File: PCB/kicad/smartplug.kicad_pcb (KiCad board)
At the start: 2 copper layers, 97.5 x 99 mm, 108 parts, among them IC9 534998-4, J1 1935174, J12 M50-3530242, J2 1935174, J3 826629-4, J7 Conn_01x01, J8 Conn_01x01, J9 USB_C_Receptacle_USB2.0, Y1 32MHZ

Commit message: PCB 1.0: - Corrected 5V generation - Corrected USB ESD protection - Replaced USB type-C with micro type-B
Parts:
- removed IC1: ~, alecot:SOT95P280X145-6N
- removed J9: USB_C_Receptacle_USB2.0, Connector_USB:USB_C_Receptacle_JAE_DX07S016JA1R1500
- removed R13: 0R, alecot:ERJ3EKF1000V
- removed R17: 10K, alecot:RESC1608X55N
- removed R19: 1M, alecot:RESC1608X55N
- removed R2: 22.1K, alecot:RESC1608X55N
- removed R20, R21: 5.1K, alecot:RESC1608X55N
- removed R3: 88.7K, alecot:RESC1608X55N
- added J4: 10118192-0002LF, alecot:101181920002LF, F.Cu at (175.4, 116.9)
- added PS2: VXO7805-1000, alecot:VXO780121000, F.Cu at (168.3, 71.9)
- C2: value 2.2u -> 10u; footprint alecot:CAPC3116X180N -> alecot:CAPC3225X270N
- C3: value 0.1u -> 22u; footprint alecot:CAPC1005X55N -> alecot:CAPC1608X90N
- C4: value 10u -> 4.7u; footprint alecot:CAPC3225X270N -> alecot:CAPC2012X135N
- L1: value 4.7u -> 12u; footprint alecot:LQM21PHR47NG0D -> alecot:1227ASH100MP2
- moved C4 14.2 mm to (173.6, 63.8), turned to 0 degrees
- moved L1 12.0 mm to (175.8, 67.5)
- moved C3 9.81 mm to (175.5, 77.6), turned to 180 degrees
- moved C2 8.33 mm to (175.8, 72.5), turned to 90 degrees
- moved C1 2.20 mm to (155.7, 76.1)
- moved G*** 1.43 mm to (169.4, 111.8)
- moved IC7 0.80 mm to (164.3, 117.2), turned to 0 degrees
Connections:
- C2 pad 2: VBUS -> Net-(PS2-+VIN)
- C3 pad 1: Net-(IC1-CB) -> GND
- C3 pad 2: Net-(IC1-SW) -> +5V
- C4 pad 2: +5V -> VBUS
- IC7 pad 1: USB_CONN_D- -> USB_D+
- IC7 pad 4: USB_D+ -> USB_CONN_D-
- L1 pad 1: Net-(IC1-SW) -> VBUS
- L1 pad 2: +5V -> Net-(PS2-+VIN)
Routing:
- net Net-(J9-SHIELD): track 24.8 -> 0.00 mm
- net +5V: track 136.6 -> 122.8 mm, vias 4 -> 3
- net GND: track 75.5 -> 67.4 mm, vias 58 -> 52
- net Net-(PS2-+VIN): track 0.00 -> 6.98 mm
- net Net-(IC1-EN): track 5.22 -> 0.00 mm
- net VBUS: track 45.9 -> 40.9 mm
- net Net-(IC1-SW): track 4.60 -> 0.00 mm
- net USB_D+: track 14.1 -> 10.1 mm
- net Net-(IC1-FB): track 3.59 -> 0.00 mm
- net Net-(J9-CC2): track 3.02 -> 0.00 mm
- net Net-(J9-CC1): track 3.02 -> 0.00 mm
- net USB_D-: track 11.0 -> 8.82 mm, vias 2 -> 0
- net USB_CONN_D+: track 6.24 -> 8.24 mm
- net Net-(IC1-CB): track 1.96 -> 0.00 mm
- net USB_CONN_D-: track 9.00 -> 8.22 mm
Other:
- board text added: "Smartplug V1.0 03/23 cotaa"
- board text removed: "Smartplug V0.0 08/23 cotaa"

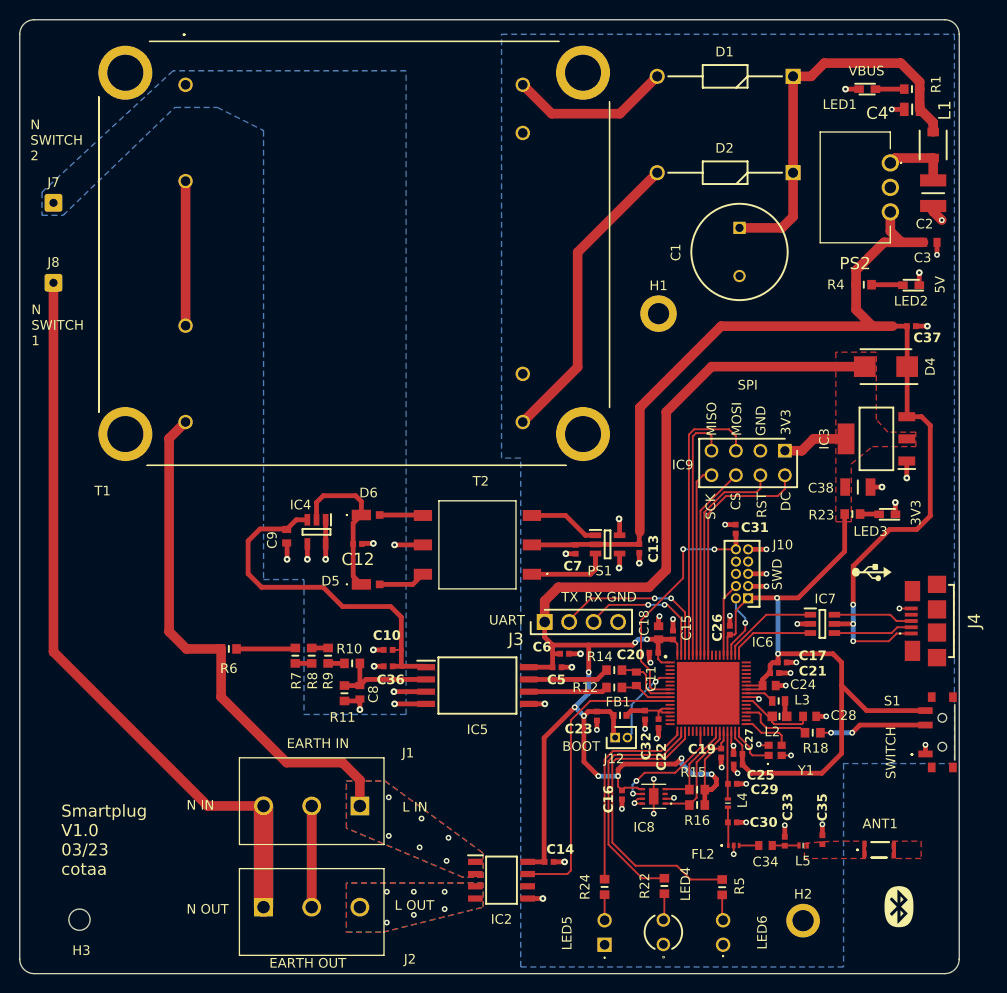
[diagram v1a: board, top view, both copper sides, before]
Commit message: Antenna chip replaced with antenna trace on PCB Switch replaced with button Added GND test point Added PD res on Boot pin Added NRST capacitor
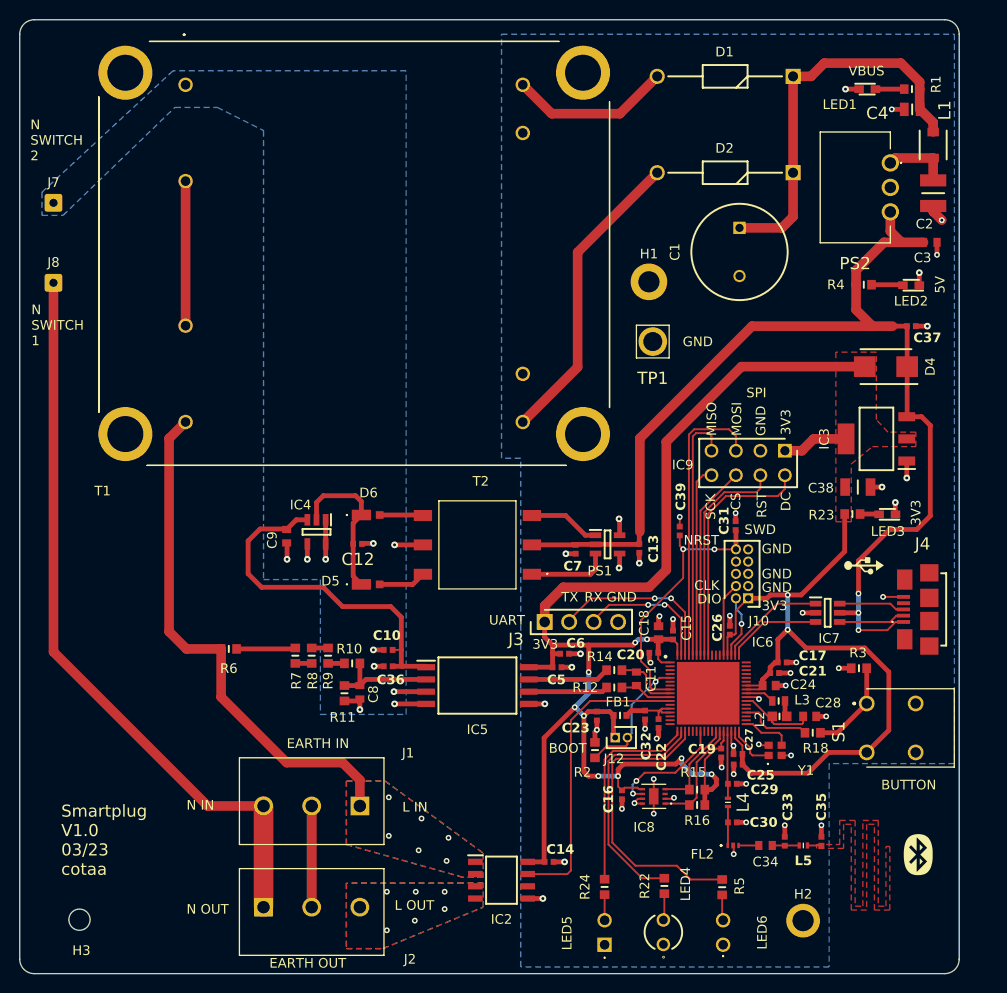
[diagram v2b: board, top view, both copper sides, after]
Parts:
- removed ANT1: ANT3216LL00R2400A, alecot:ANT3216LL00R2400A
- added C39: 0.1u, alecot:CAPC1005X55N, F.Cu at (149.5, 107.6)
- added R2: 10K, alecot:RESC1608X55N, F.Cu at (140.7, 130.3)
- added R3: 10K, alecot:RESC1608X55N, F.Cu at (168.1, 121.8)
- added TP1: 5023, alecot:5023, F.Cu at (146.7, 87.9)
- C35: value n.f. -> 1.2p
- L5: value 0L -> 3.6n
- S1: value PCM12SMTR -> 800SP9B5M6RE; footprint alecot:PCM12SMTR -> alecot:800SP9B5M6RE
- moved S1 8.40 mm to (168.9, 125.5), turned to -90 degrees
- moved G*** 5.76 mm to (174.2, 141.1)
- moved H1 3.45 mm to (146.3, 81.7)
- moved J4 1.44 mm to (174.6, 115.7)
- moved IC7 1.27 mm to (164.8, 116.0)
- moved G*** 1.06 mm to (168.6, 111.1)
- moved C31 0.36 mm to (155.3, 107.0)
- moved C35 0.19 mm to (164.2, 139.8), turned to -90 degrees
- moved L4 0.08 mm to (154.5, 135.7)
- moved FL2 0.06 mm to (155.0, 140.2)
- turned L5 to 0 degrees
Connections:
- C35 pad 1: /interfaces/FEED -> GND
- C35 pad 2: GND -> /interfaces/FEED
- L5 pad 1: /interfaces/FEED -> /interfaces/MATCH_IMP
- L5 pad 2: /interfaces/MATCH_IMP -> /interfaces/FEED
- S1 pad 1: GND -> SW_SWITCH
- S1 pad 2: SW_SWITCH -> GND
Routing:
- net BOOT: track 8.74 -> 13.4 mm
- net +5V: track 122.8 -> 118.2 mm
- net +3.3V: track 235.8 -> 233.0 mm
- net GND: track 67.4 -> 65.1 mm, vias 52 -> 50
- net NRST: track 25.8 -> 27.4 mm
- net SW_SWITCH: track 11.2 -> 9.72 mm, vias 2 -> 0
- net /interfaces/FEED: track 0.00 -> 1.46 mm
- net USB_CONN_D+: track 8.24 -> 6.87 mm
- net USB_CONN_D-: track 8.22 -> 6.89 mm
- net USB_D+: track 10.1 -> 11.1 mm
- net USB_D-: track 8.82 -> 9.85 mm
- removed copper zone on F.Cu, net /interfaces/SOLD
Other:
- board text added: "BUTTON"
- board text added: "CLK"
- board text added: "DIO"
- board text added: "NRST"
- board text removed: "SWITCH"

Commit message: Modified year silk
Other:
- board text added: "Smartplug V1.0 03/24 cotaa"
- board text removed: "Smartplug V1.0 03/23 cotaa"
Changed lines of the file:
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@@
     (effects (font (size 1 1) (thickness 0.15)) (justify left bottom))
   )
-  (gr_text "Smartplug\nV1.0\n03/23\ncotaa" (at 85.3 143.4) (layer "F.SilkS")
+  (gr_text "Smartplug\nV1.0\n03/24\ncotaa" (at 85.3 143.4) (layer "F.SilkS")
     (effects (font (size 1.25 1.25) (thickness 0.2)) (justify left bottom))
   )

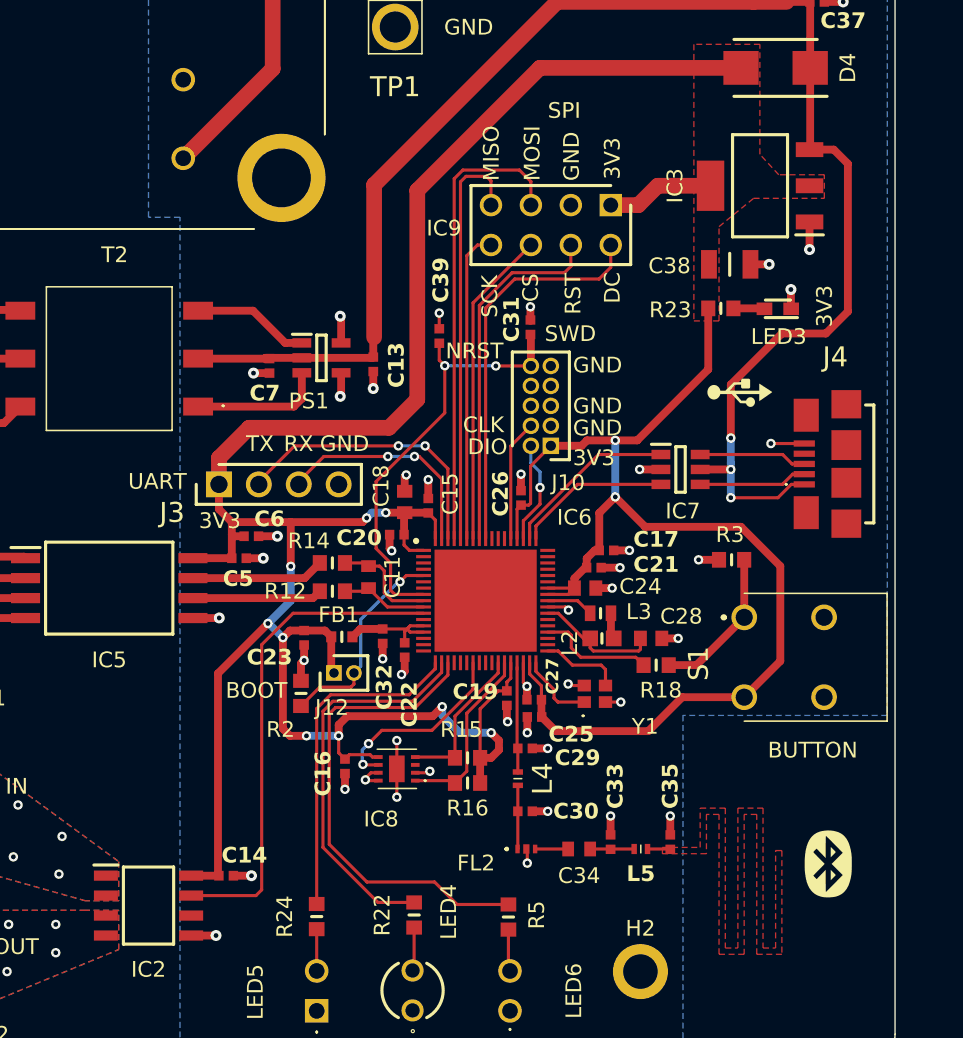
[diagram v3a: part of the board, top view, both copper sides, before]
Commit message: Added some test points
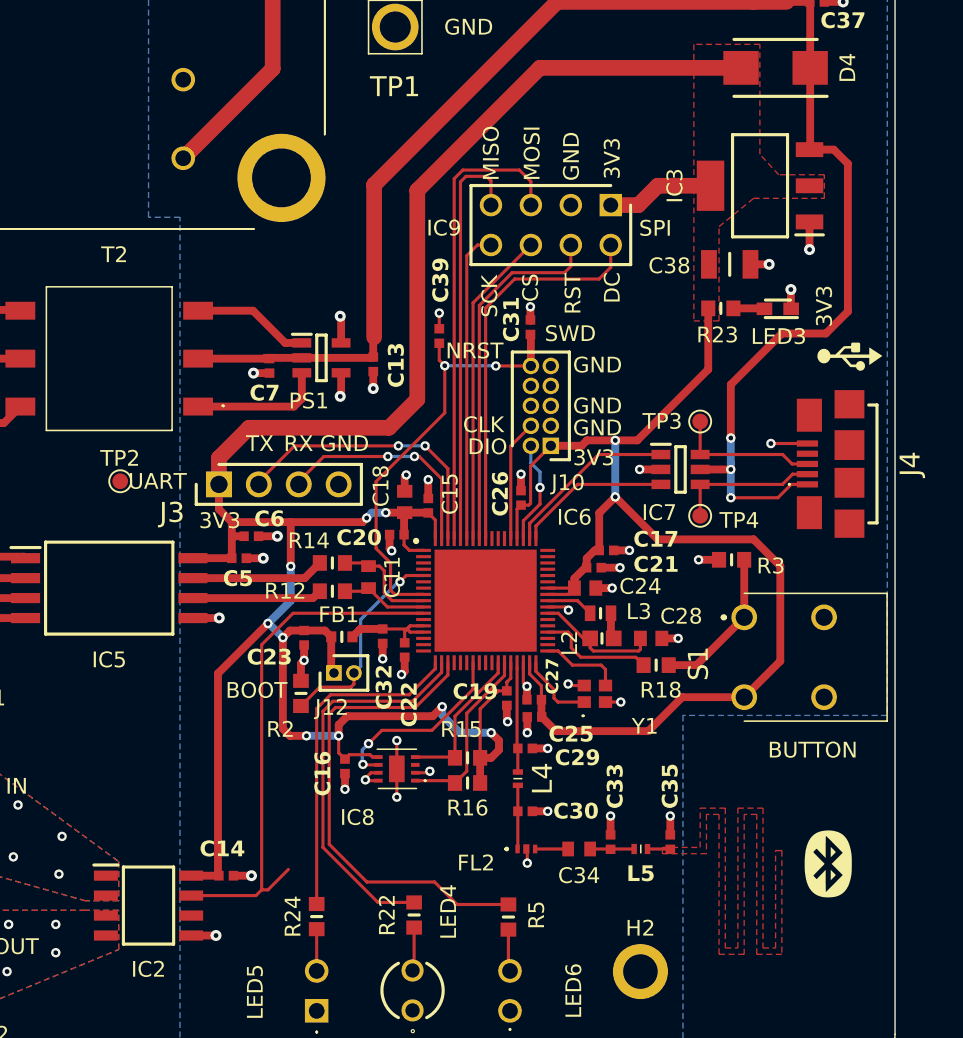
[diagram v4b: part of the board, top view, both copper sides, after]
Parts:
- added TP2: TestPoint, TestPoint:TestPoint_Pad_D1.0mm, F.Cu at (129.2, 116.8)
- added TP3: TestPoint, TestPoint:TestPoint_Pad_D1.0mm, F.Cu at (166.1, 113.0)
- added TP4: TestPoint, TestPoint:TestPoint_Pad_D1.0mm, F.Cu at (166.1, 119.0)
- moved G*** 7.37 mm to (175.6, 108.8)
- moved J4 0.20 mm to (174.8, 115.7)
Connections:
- J4 pad MP1: (no net) -> unconnected-(J4-MP-PadMP1)
- J4 pad MP2: (no net) -> unconnected-(J4-MP-PadMP2)
- J4 pad MP3: (no net) -> unconnected-(J4-MP-PadMP3)
- J4 pad MP4: (no net) -> unconnected-(J4-MP-PadMP4)
- J4 pad MP5: (no net) -> unconnected-(J4-MP-PadMP5)
- J4 pad MP6: (no net) -> unconnected-(J4-MP-PadMP6)
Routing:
- net USB_CONN_D+: track 6.87 -> 9.17 mm
- net AN_IIN: track 31.4 -> 33.6 mm
- net USB_CONN_D-: track 6.89 -> 9.09 mm
